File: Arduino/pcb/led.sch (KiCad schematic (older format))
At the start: 3 parts, among them U4 74HC595

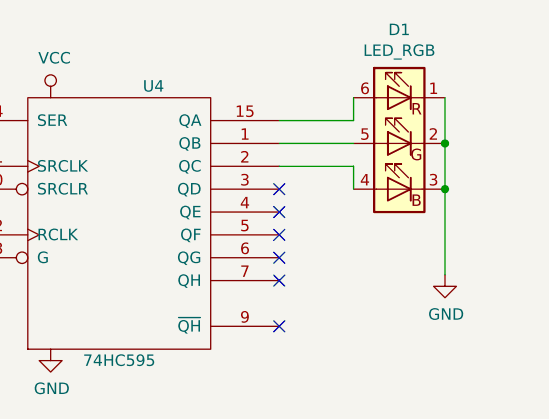
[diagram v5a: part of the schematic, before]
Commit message: pcb: add led series resistors to rgb led
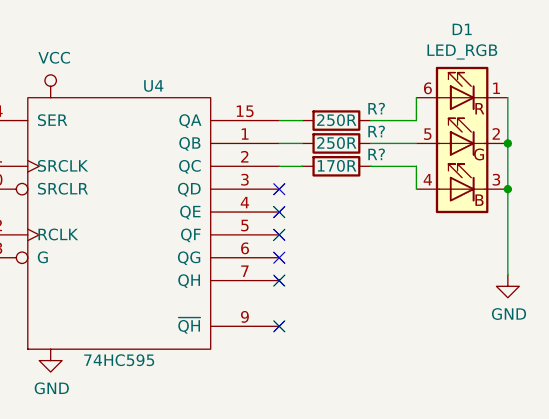
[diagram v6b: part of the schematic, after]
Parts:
- added R? (x2): 250R, symbol Device:R
- added R?: 170R, symbol Device:R
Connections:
- net at D1.4 (BA): now also R?.1; no longer U4.2 (QC)
- net at D1.5 (GA): now also R?.1; no longer U4.1 (QB)
- net at D1.6 (RA): now also R?.1; no longer U4.15 (QA)
- new net: R?.2, U4.1 (QB)
- new net: R?.2, U4.15 (QA)
- new net: R?.2, U4.2 (QC)
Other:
- moved on the sheet: D1
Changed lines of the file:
@@
 L Device:LED_RGB D1
 U 1 1 5D09B2AA
-P 6700 3050
-F 0 "D1" H 6700 3547 50  0000 C CNN
-F 1 "LED_RGB" H 6700 3456 50  0000 C CNN
-F 2 "LED_SMD:LED_RGB_1210" H 6700 3000 50  0001 C CNN
-F 3 "~" H 6700 3000 50  0001 C CNN
-	1    6700 3050
+P 6975 3050
+F 0 "D1" H 6975 3547 50  0000 C CNN
+F 1 "LED_RGB" H 6975 3456 50  0000 C CNN
+F 2 "LED_SMD:LED_RGB_1210" H 6975 3000 50  0001 C CNN
+F 3 "~" H 6975 3000 50  0001 C CNN
+	1    6975 3050
 	-1   0    0    -1
 $EndComp
@@
 L power:GND #PWR039
 U 1 1 5D09B2B0
-P 6900 3625
-F 0 "#PWR039" H 6900 3375 50  0001 C CNN
-F 1 "GND" H 6905 3452 50  0000 C CNN
-F 2 "" H 6900 3625 50  0001 C CNN
-F 3 "" H 6900 3625 50  0001 C CNN
-	1    6900 3625
+P 7175 3625
+F 0 "#PWR039" H 7175 3375 50  0001 C CNN
+F 1 "GND" H 7180 3452 50  0000 C CNN
+F 2 "" H 7175 3625 50  0001 C CNN
+F 3 "" H 7175 3625 50  0001 C CNN
+	1    7175 3625
 	1    0    0    -1
 $EndComp
+Connection ~ 7175 3050
+Connection ~ 7175 3250
 Wire Wire Line
-	6175 2950 6500 2950
+	6775 2950 6775 2850
 Wire Wire Line
-	6175 3050 6500 3050
-Connection ~ 6900 3050
-Connection ~ 6900 3250
+	7175 3050 7175 3250
 Wire Wire Line
-	6500 2950 6500 2850
+	7175 3250 7175 3625
 Wire Wire Line
-	6900 3050 6900 3250
+	6775 3150 6775 3250
 Wire Wire Line
-	6900 3250 6900 3625
-Wire Wire Line
-	6500 3150 6500 3250
-Wire Wire Line
-	6175 3150 6500 3150
-Wire Wire Line
-	6900 2850 6900 3050
+	7175 2850 7175 3050
 $Comp
 L power:GND #PWR036
@@
 Text Notes 3375 2950 0    50   ~ 0
 Bypass
+$Comp
+L Device:R R?
+U 1 1 5CDFA92E
+P 6425 3050
+F 0 "R?" V 6375 3225 50  0000 C CNN
+F 1 "250R" V 6425 3050 50  0000 C CNN
+F 2 "" V 6355 3050 50  0001 C CNN
+F 3 "~" H 6425 3050 50  0001 C CNN
+	1    6425 3050
+	0    1    1    0
+$EndComp
+$Comp
+L Device:R R?
+U 1 1 5CDFACA1
+P 6425 2950
+F 0 "R?" V 6375 3125 50  0000 C CNN
+F 1 "250R" V 6425 2950 50  0000 C CNN
+F 2 "" V 6355 2950 50  0001 C CNN
+F 3 "~" H 6425 2950 50  0001 C CNN
+	1    6425 2950
+	0    1    1    0
+$EndComp
+$Comp
+L Device:R R?
+U 1 1 5CDFAF66
+P 6425 3150
+F 0 "R?" V 6375 3325 50  0000 C CNN
+F 1 "170R" V 6425 3150 50  0000 C CNN
+F 2 "" V 6355 3150 50  0001 C CNN
+F 3 "~" H 6425 3150 50  0001 C CNN
+	1    6425 3150
+	0    1    1    0
+$EndComp
+Wire Wire Line
+	6175 2950 6275 2950
+Wire Wire Line
+	6175 3050 6275 3050
+Wire Wire Line
+	6175 3150 6275 3150
+Wire Wire Line
+	6575 2950 6775 2950
+Wire Wire Line
+	6575 3050 6775 3050
+Wire Wire Line
+	6575 3150 6775 3150
 $EndSCHEMATC

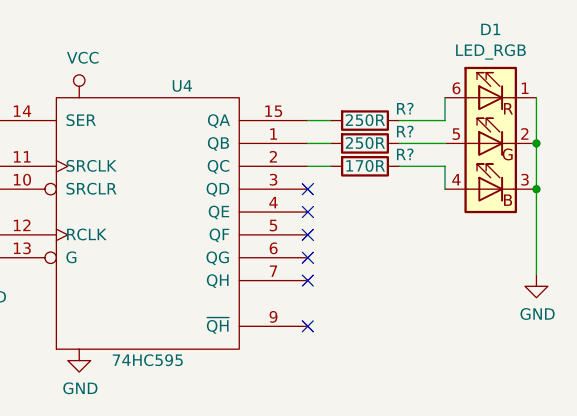
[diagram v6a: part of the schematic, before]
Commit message: pcb: add missing footprints / add component for logo footprint
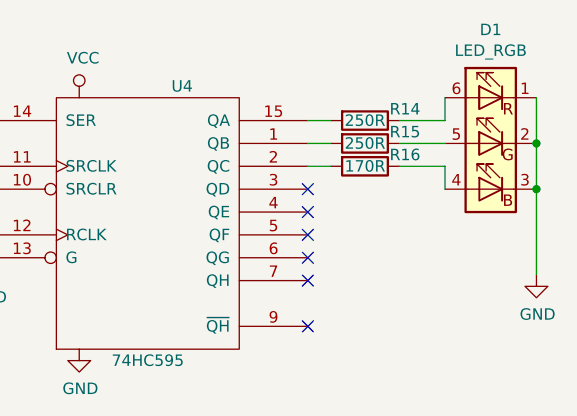
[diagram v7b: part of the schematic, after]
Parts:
- R14, R15, R16: renamed from R?; footprint (none) -> Resistor_SMD:R_0805_2012Metric
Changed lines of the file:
@@
 Bypass
 $Comp
-L Device:R R?
+L Device:R R15
 U 1 1 5CDFA92E
 P 6425 3050
-F 0 "R?" V 6375 3225 50  0000 C CNN
+F 0 "R15" V 6375 3225 50  0000 C CNN
 F 1 "250R" V 6425 3050 50  0000 C CNN
-F 2 "" V 6355 3050 50  0001 C CNN
+F 2 "Resistor_SMD:R_0805_2012Metric" V 6355 3050 50  0001 C CNN
 F 3 "~" H 6425 3050 50  0001 C CNN
 	1    6425 3050
@@
 $EndComp
 $Comp
-L Device:R R?
+L Device:R R14
 U 1 1 5CDFACA1
 P 6425 2950
-F 0 "R?" V 6375 3125 50  0000 C CNN
+F 0 "R14" V 6375 3125 50  0000 C CNN
 F 1 "250R" V 6425 2950 50  0000 C CNN
-F 2 "" V 6355 2950 50  0001 C CNN
+F 2 "Resistor_SMD:R_0805_2012Metric" V 6355 2950 50  0001 C CNN
 F 3 "~" H 6425 2950 50  0001 C CNN
 	1    6425 2950
@@
 $EndComp
 $Comp
-L Device:R R?
+L Device:R R16
 U 1 1 5CDFAF66
 P 6425 3150
-F 0 "R?" V 6375 3325 50  0000 C CNN
+F 0 "R16" V 6375 3325 50  0000 C CNN
 F 1 "170R" V 6425 3150 50  0000 C CNN
-F 2 "" V 6355 3150 50  0001 C CNN
+F 2 "Resistor_SMD:R_0805_2012Metric" V 6355 3150 50  0001 C CNN
 F 3 "~" H 6425 3150 50  0001 C CNN
 	1    6425 3150

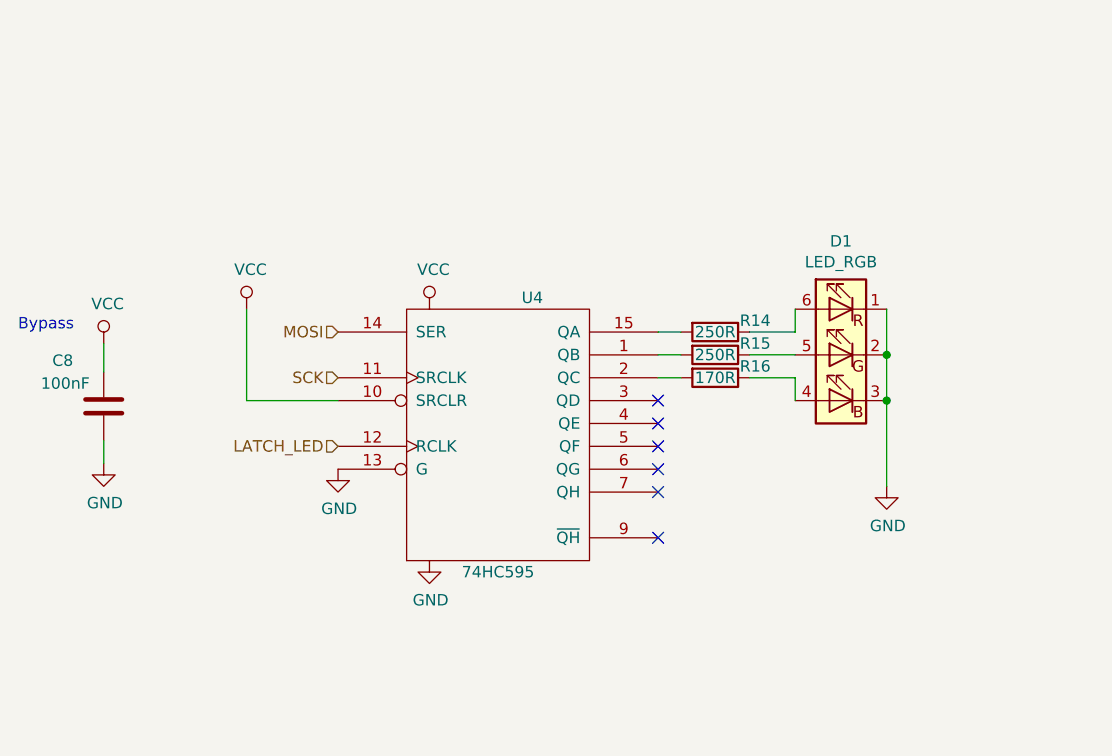
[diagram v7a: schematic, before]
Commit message: pcb: add mosfets to RGB led
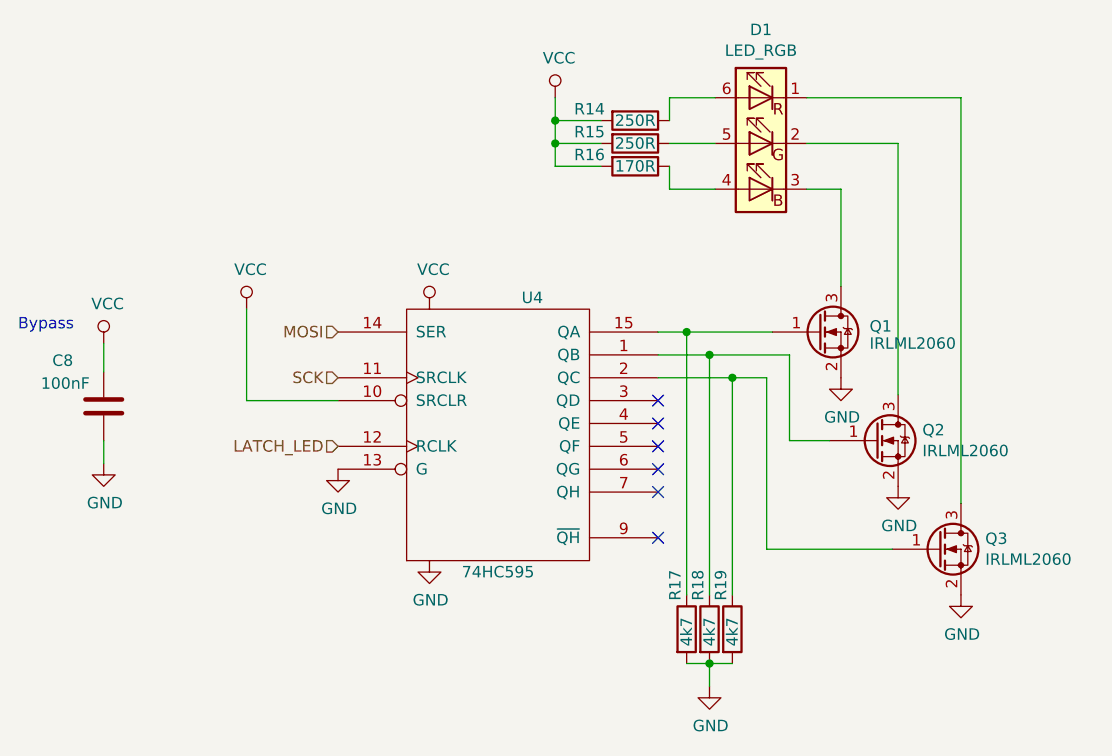
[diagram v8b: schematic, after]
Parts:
- added Q1, Q2, Q3: IRLML2060, Package_TO_SOT_SMD:SOT-23, symbol Transistor_FET:IRLML2060
- added R17, R18, R19: 4k7, Resistor_SMD:R_0805_2012Metric, symbol Device:R
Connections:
- net GND: now also Q1.2 (S), Q2.2 (S), Q3.2 (S), R17.2, R18.2, R19.2; no longer D1.1 (RK), D1.2 (GK), D1.3 (BK)
- net VCC: now also R14.2, R15.2, R16.2
- net at U4.1 (QB): now also Q2.1 (G), R18.1; no longer R15.2
- net at U4.15 (QA): now also Q1.1 (G), R17.1; no longer R14.2
- net at U4.2 (QC): now also Q3.1 (G), R19.1; no longer R16.2
- new net: D1.3 (BK), Q1.3 (D)
- new net: D1.2 (GK), Q2.3 (D)
- new net: D1.1 (RK), Q3.3 (D)
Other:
- moved on the sheet: D1, R14, R15, R16
